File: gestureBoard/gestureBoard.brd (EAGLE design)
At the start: 10.1 x 13.6 mm, 11 parts, among them J1 GRPB042MWCN-RC, U1 APDS-9960

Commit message: more progress on routing
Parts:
- added U3: PCA9553TSSOP8, glasses:SOP65P490X110-8
- moved R3 2.33 mm to (6.10, 3.61), flipped to the bottom, turned to 0 degrees
- moved R2 1.83 mm to (6.55, 1.73), flipped to the bottom, turned to 270 degrees
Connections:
- net +3V3: now also U3.8
- net GND: now also U3.4
- net LED_B: now also U3.3; no longer J1.4
- net LED_G: now also U3.2; no longer J1.3
- net LED_R: now also U3.1; no longer J1.5
- net SCL: now also U3.6
- net SDA: now also U3.7
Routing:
- net SCL: track 12.4 -> 24.1 mm
- net SDA: track 4.58 -> 13.1 mm
- net LED_R: track 1.41 -> 5.88 mm, vias 0 -> 1
- net LED_B: track 2.12 -> 5.08 mm
- net +3V3: track 25.6 -> 27.2 mm
- net LED_G: track 6.36 -> 5.26 mm
- net N$2: track 1.90 -> 1.33 mm, vias 0 -> 1
- net N$3: track 1.67 -> 1.50 mm, vias 0 -> 1
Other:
- board size 10.1 x 13.6 mm -> 9.2 x 13.6 mm

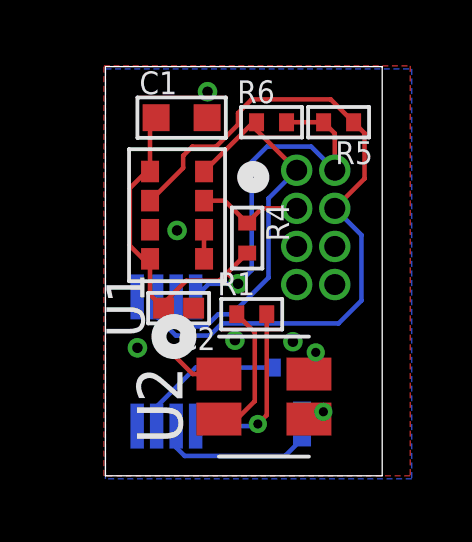
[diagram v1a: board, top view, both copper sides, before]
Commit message: made more progress on routing, and added capacitive touch slider board
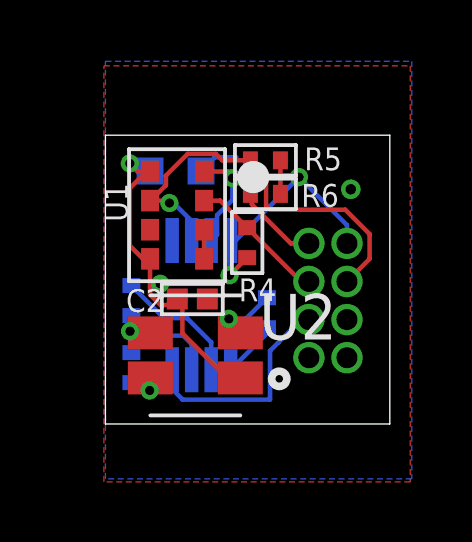
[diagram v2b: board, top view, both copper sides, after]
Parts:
- moved R2 7.02 mm to (0.86, 5.84), turned to 90 degrees
- moved R3 5.23 mm to (0.86, 3.61), turned to 90 degrees
- moved R5 2.75 mm to (5.33, 10.5), turned to 0 degrees
- moved U2 2.67 mm to (3.00, 4.01), turned to 90 degrees
- moved J1 2.47 mm to (7.42, 5.84)
- moved R6 2.40 mm to (5.33, 9.40)
- moved U3 2.21 mm to (3.20, 5.69)
- moved C1 1.79 mm to (2.34, 10.2), flipped to the bottom, turned to 180 degrees
- moved C2 0.55 mm to (2.90, 5.89)
- moved R1 0.51 mm to (5.38, 5.44), flipped to the bottom, turned to 270 degrees
- moved R4 0.15 mm to (4.72, 7.77)
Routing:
- net SCL: track 24.1 -> 14.0 mm, vias 0 -> 1
- net GND: track 0.00 -> 8.78 mm, vias 5 -> 1
- net SDA: track 13.1 -> 7.31 mm, vias 0 -> 1
- net LED_R: track 5.88 -> 1.90 mm, vias 1 -> 0
- net N$1: track 4.59 -> 2.19 mm, vias 0 -> 1
- net +3V3: track 27.2 -> 25.1 mm, vias 1 -> 4
- net LED_B: track 5.08 -> 3.22 mm
- net INT: track 3.60 -> 4.61 mm
- net LED_G: track 5.26 -> 4.36 mm
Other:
- board size 9.2 x 13.6 mm -> 9.5 x 9.6 mm
